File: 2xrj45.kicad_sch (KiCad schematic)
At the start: 20 parts, among them J1 Bus_RJ45_JTH-0024NL, J2 Bus_RJ45_JTH-0024NL

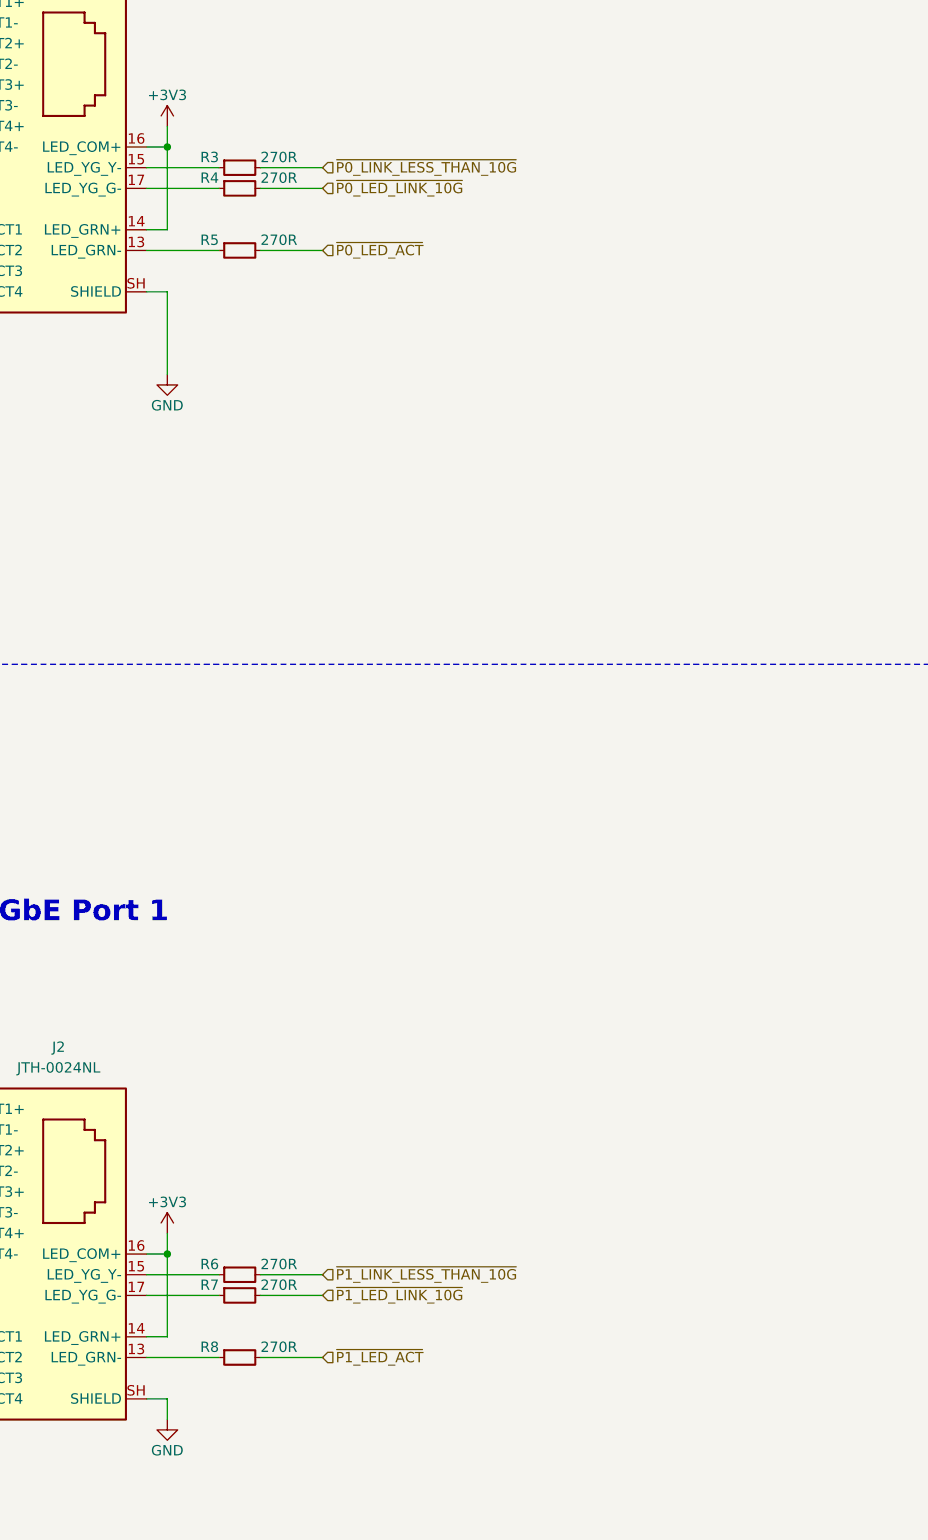
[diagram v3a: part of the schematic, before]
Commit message: [#80813] WIP: Adjust passives values, add missing load capacitors for the 50MHz resonator
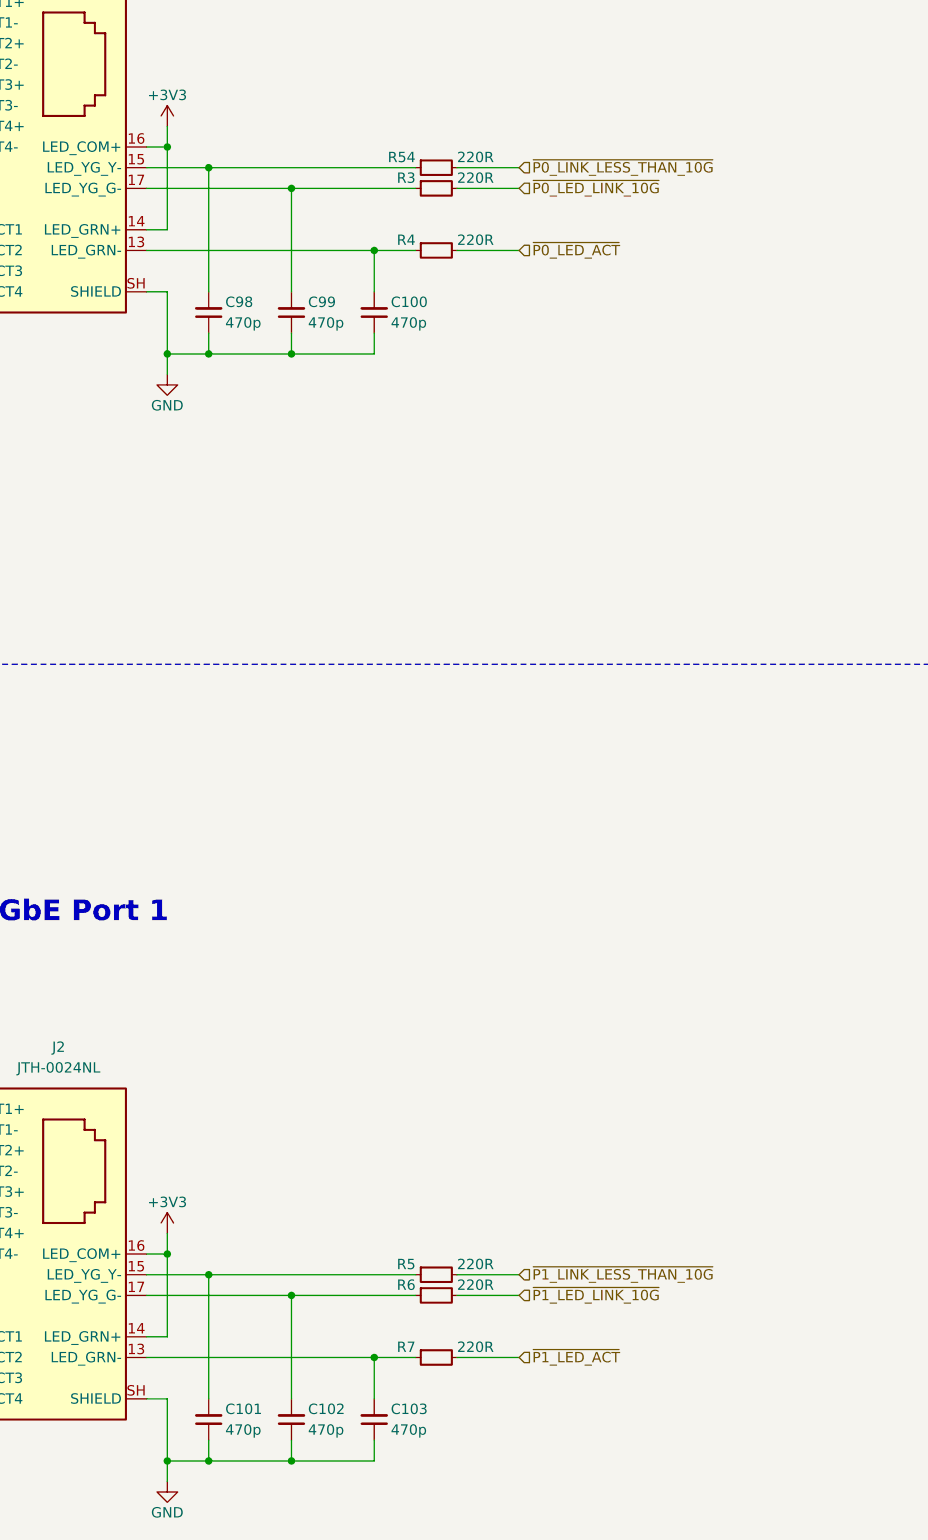
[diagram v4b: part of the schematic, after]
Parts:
- removed R3, R4, R5, R6, R7, R8: R_270R_0402, antmicro-footprints:R_0402_1005Metric, symbol antmicroResistors0402:R_270R_0402
- added C100, C101, C102, C103, C98, C99: C_470p_0402, antmicro-footprints:C_0402_1005Metric, symbol antmicroCapacitors0402:C_470p_0402
- added R3, R4, R5, R54, R6, R7: R_220R_0402, antmicro-footprints:R_0402_1005Metric, symbol antmicroResistors0402:R_220R_0402
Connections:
- net GND: now also C100.1, C101.1, C102.1, C103.1, C98.1, C99.1
- net ~{P0_LED_ACT}: now also R4.2
- net ~{P0_LED_LINK_10G}: now also R3.2
- net ~{P0_LINK_LESS_THAN_10G}: now also R54.2
- net ~{P1_LED_ACT}: now also R7.2
- net ~{P1_LED_LINK_10G}: now also R6.2
- net ~{P1_LINK_LESS_THAN_10G}: now also R5.2
- net at J2.13 (LED_GRN-): now also C103.2, R7.1
- net at J2.15 (LED_YG_Y-): now also C101.2, R5.1
- net at J2.17 (LED_YG_G-): now also C102.2, R6.1
- net at J1.17 (LED_YG_G-): now also C99.2, R3.1
- net at J1.13 (LED_GRN-): now also C100.2, R4.1
- net at J1.15 (LED_YG_Y-): now also C98.2, R54.1

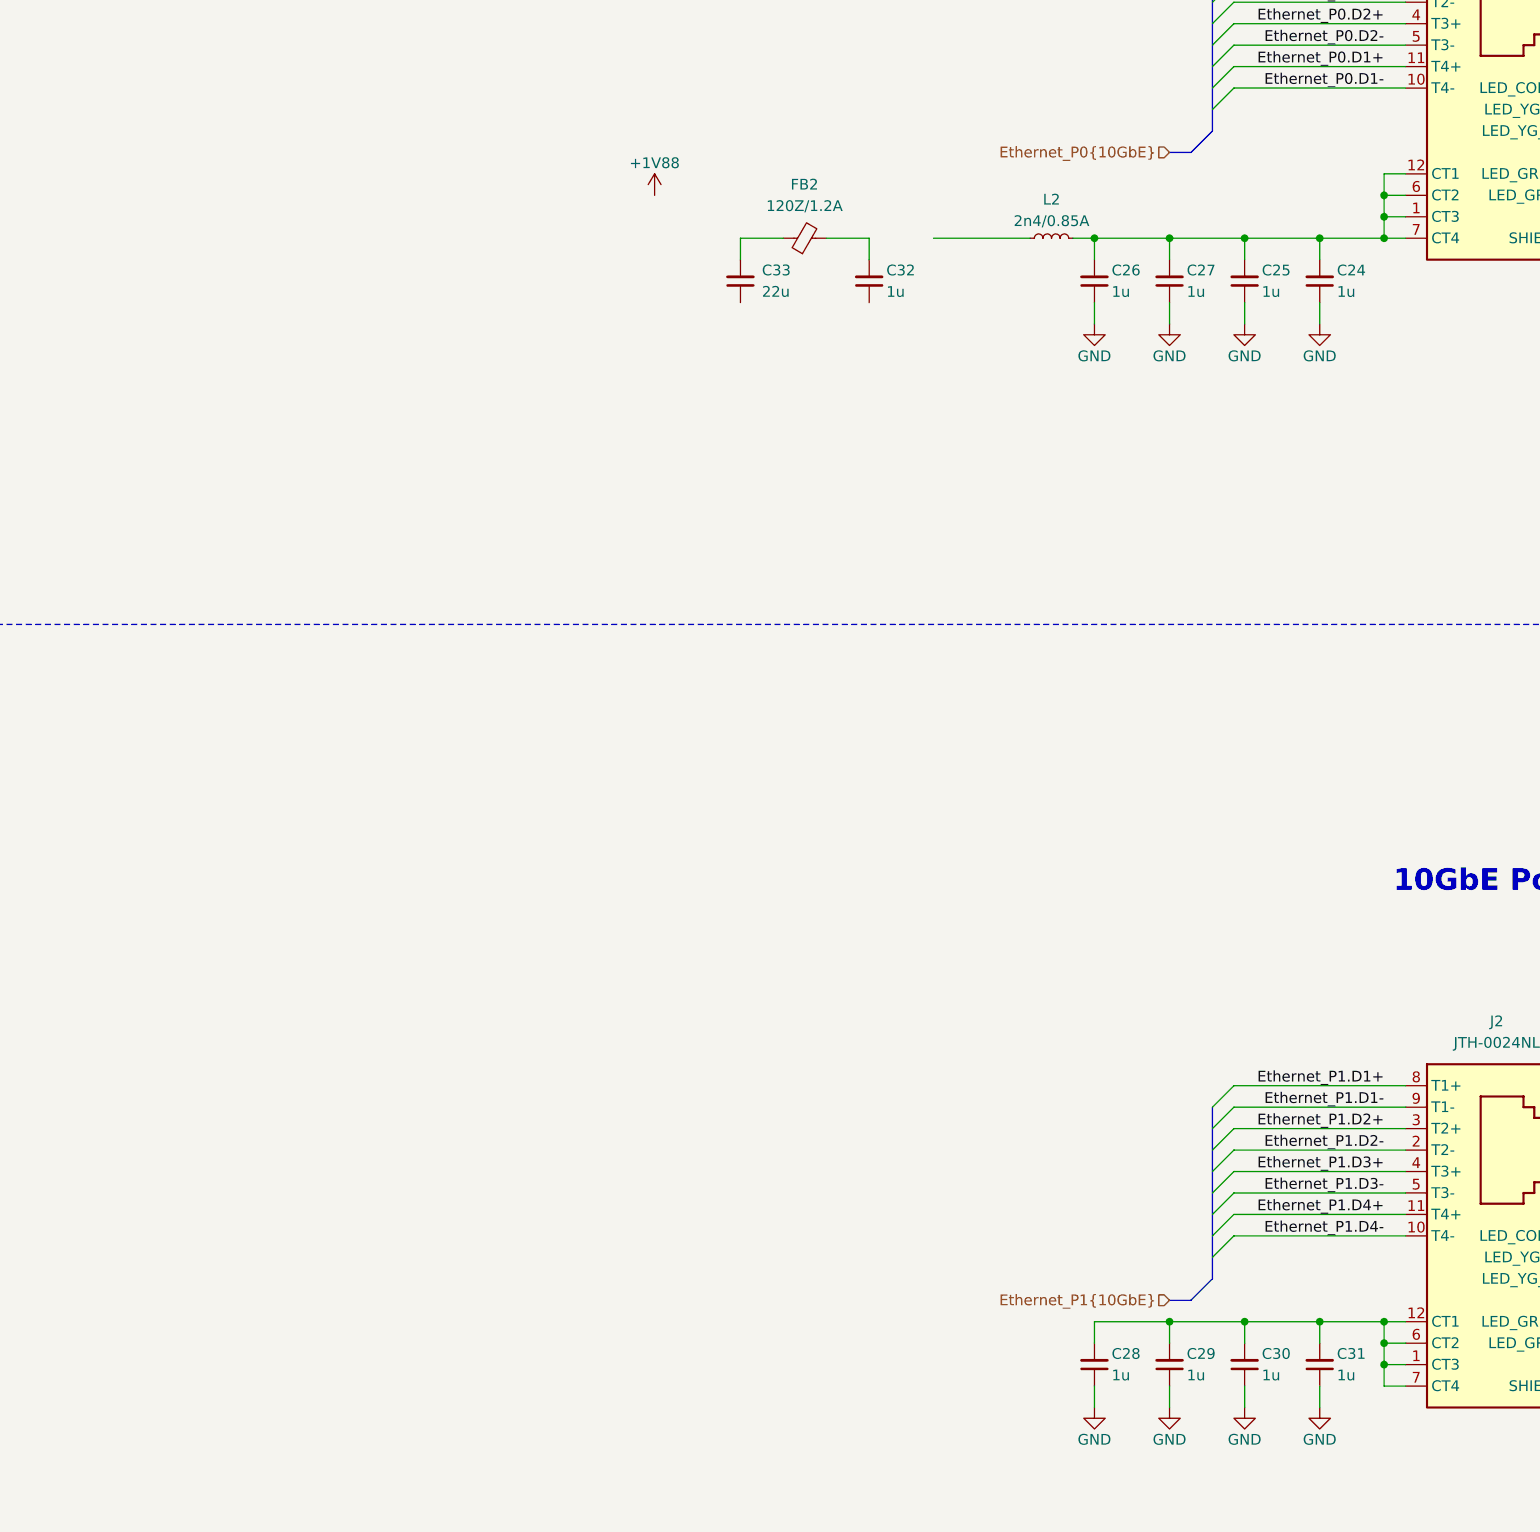
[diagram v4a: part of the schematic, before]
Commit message: [#80813] Adjust passives values, add remaining decoupling capacitors
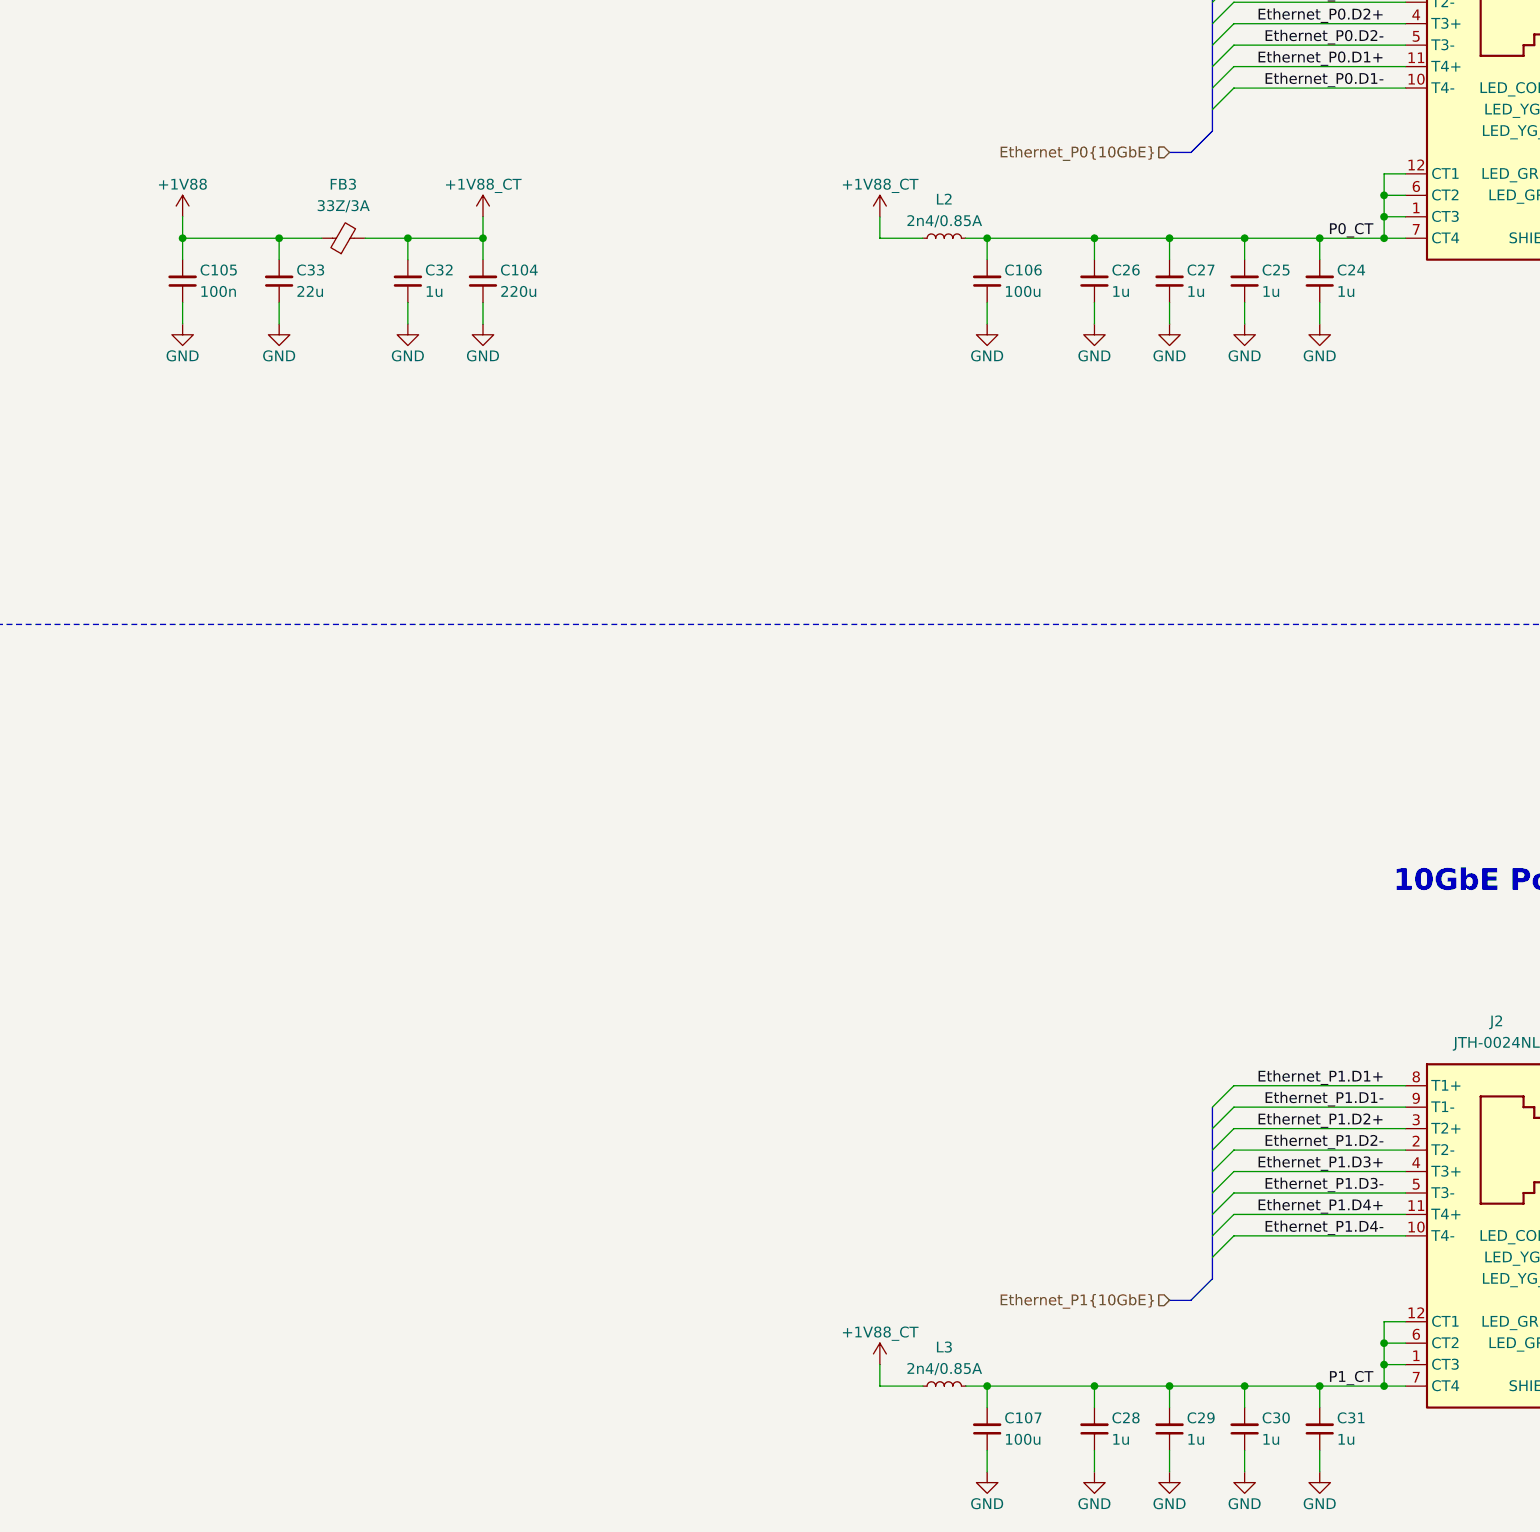
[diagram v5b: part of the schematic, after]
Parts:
- removed FB2: FB_120Z_1.2A_TDK-MPZ_0402, antmicro-footprints:FB_0402_1005Metric, symbol antmicroFerriteBeadsandChips:FB_120Z_1.2A_TDK-MPZ_0402
- added C104: C_220u_1206_6V3, antmicro-footprints:C_1206_3216Metric, symbol antmicroCapacitorsmisc:C_220u_1206_6V3
- added C105: C_100n_16V_X7R_0402, antmicro-footprints:C_0402_1005Metric, symbol antmicroCapacitors0402:C_100n_16V_X7R_0402
- added C106, C107: C_100u_0805, antmicro-footprints:C_0805_2012Metric, symbol antmicroCapacitorsmisc:C_100u_0805
- added FB3: FB_33Z_3A_Murata-BLM18PG_0603, antmicro-footprints:FB_0603_1608Metric, symbol antmicroFerriteBeadsandChips:FB_33Z_3A_Murata-BLM18PG_0603
- added L3: L_2n4_0.85A_0402, antmicro-footprints:L_0402_1005Metric, symbol antmicroFixedInductors:L_2n4_0.85A_0402
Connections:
- net +1V88: now also C33.2, C105.2, FB3.1
- net GND: now also C32.1, C33.1, C104.1, C105.1, C106.1, C107.1
- net P0_CT: now reaches C24.2, C25.2, C26.2, C27.2, J1.1 (CT3), J1.12 (CT1), J1.6 (CT2), J1.7 (CT4), L2.2
- net P0_CT: now also C106.2
- net P1_CT: now reaches C28.2, C29.2, C30.2, C31.2, J2.1 (CT3), J2.12 (CT1), J2.6 (CT2), J2.7 (CT4)
- net P1_CT: now also C107.2, L3.2
- net +1V88_CT: now reaches C32.2
- net +1V88_CT: now also L2.1, C104.2, FB3.2, L3.1
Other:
- moved on the sheet: C28, C29, C30, C31, C32, C33, L2
